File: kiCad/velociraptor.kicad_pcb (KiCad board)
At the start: 2 copper layers, 218 x 86.6 mm, 125 parts, among them J0 Conn_01x03, SW0 MX, SW1 MX, SW10 MX, SW11 MX, SW12 MX, SW13 MX, SW14 MX, SW15 MX, SW16 MX, SW17 MX, SW18 MX, SW19 MX, SW2 MX, SW20 MX, SW21 MX, SW22 MX, SW23 MX, SW24 MX, SW25 MX, SW26 MX, SW27 MX, SW28 MX, SW29 MX, SW3 MX, SW30 MX, SW31 MX, SW32 MX, SW33 MX, SW34 MX, SW35 MX, SW36 MX, SW37 MX, SW38 MX, SW39 MX, SW4 MX, SW40 MX, SW41 MX, SW42 MX, SW43 MX, SW44 MX, SW45 MX, SW46 MX, SW47 MX, SW48 MX, SW49 MX, SW5 MX, SW50 MX, SW51 MX, SW52 MX, SW53 MX, SW54 MX, SW55 MX, SW56 MX, SW57 MX, SW58 MX, SW59 MX, SW6 MX, SW61 MX, SW7 MX, SW8 MX, SW9 MX, U0 Sparkfun_Pro_Micro

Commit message: remove unused libraries, update to kicad 7, cleanup silkscreens
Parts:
- added ?: , , F.Cu at (232.5, 94.4)
- added ?: , , F.Cu at (51.9, 94.4)
- added ?: , , F.Cu at (51.9, 43.2)
- added ?: , , F.Cu at (142.3, 60.3)
- added ?: , , F.Cu at (232.5, 43.2)
- added ?: , , F.Cu at (142.3, 94.4)
- moved G*** 0.26 mm to (210.5, 90.7)
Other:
- board text added: "Velociraptor PCB by SylivanKenobi"

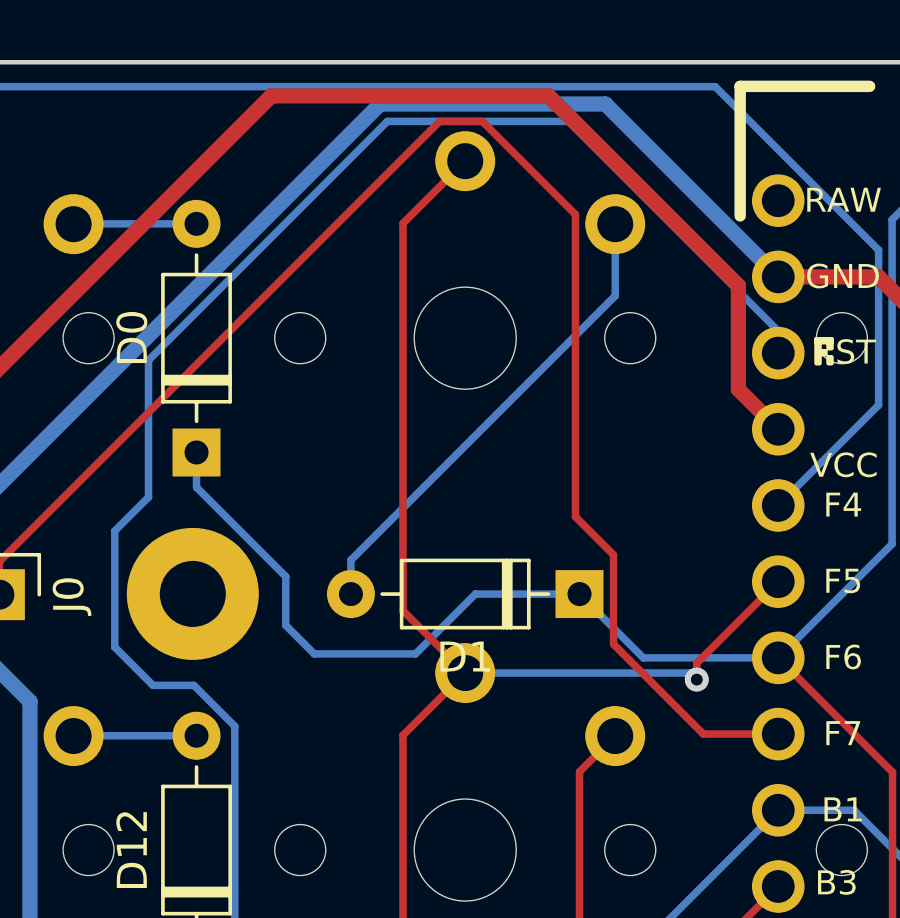
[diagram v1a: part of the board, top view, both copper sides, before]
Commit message: fix diode orientation
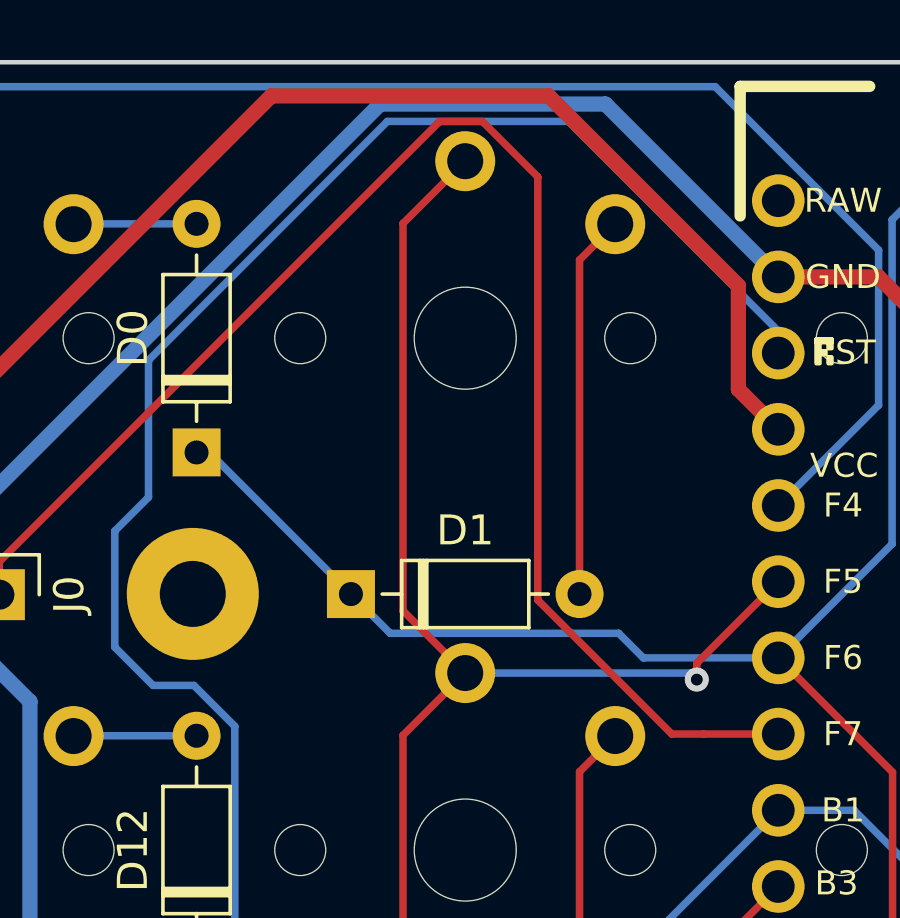
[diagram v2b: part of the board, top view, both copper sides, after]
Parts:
- moved D1 7.62 mm to (57.2, 43.2), turned to 0 degrees
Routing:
- net /ROW0: track 228.1 -> 224.8 mm
- net Net-(D1-A): track 16.0 -> 12.8 mm
- net /PIN15: track 49.2 -> 49.9 mm
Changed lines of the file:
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@@
   (net 82 "unconnected-(U0-RAW-Pad24)")
   (footprint "Diode_THT:D_DO-35_SOD27_P7.62mm_Horizontal" (layer "F.Cu")
-    (at 64.816199 43.23 180)
+    (at 57.196199 43.23)
     (descr "Diode, DO-35_SOD27 series, Axial, Horizontal, pin pitch=7.62mm, , length*diameter=4*2mm^2, , http://www.diodes.com/_files/packages/DO-35.pdf")
     (tags "Diode DO-35_SOD27 series Axial Horizontal pin pitch 7.62mm  length 4mm diameter 2mm")
@@
     (fp_line (start 7.62 0) (end 5.81 0)
       (stroke (width 0.1) (type solid)) (layer "F.Fab"))
-    (pad "1" thru_hole rect (at 0 0 180) (size 1.6 1.6) (drill 0.8) (layers "*.Cu" "*.Mask")
+    (pad "1" thru_hole rect (at 0 0) (size 1.6 1.6) (drill 0.8) (layers "*.Cu" "*.Mask")
       (net 16 "/ROW0") (pinfunction "K") (pintype "passive"))
-    (pad "2" thru_hole oval (at 7.62 0 180) (size 1.6 1.6) (drill 0.8) (layers "*.Cu" "*.Mask")
+    (pad "2" thru_hole oval (at 7.62 0) (size 1.6 1.6) (drill 0.8) (layers "*.Cu" "*.Mask")
       (net 22 "Net-(D1-A)") (pinfunction "A") (pintype "passive"))
     (model "${KICAD6_3DMODEL_DIR}/Diode_THT.3dshapes/D_DO-35_SOD27_P7.62mm_Horizontal.wrl"
@@
     (effects (font (size 1.5 1.5) (thickness 0.3) bold) (justify left bottom mirror))
   )
-  (dimension (type aligned) (layer "F.Cu")
-    (pts (xy 248.866202 112.147453) (xy 248.866202 25.502547))
-    (height 8.908798)
-    (gr_text "86.6449 mm" (at 255.975 68.825 90) (layer "F.Cu")
-      (effects (font (size 1.5 1.5) (thickness 0.3)))
+  (dimension (type aligned) (layer "Dwgs.User")
+    (pts (xy 232.495619 94.3875) (xy 142.278099 94.3875))
+    (height -24.7125)
+    (gr_text "90.2175 mm" (at 187.386859 117.95) (layer "Dwgs.User")
+      (effects (font (size 1 1) (thickness 0.15)))
+    )
+    (format (prefix "") (suffix "") (units 3) (units_format 1) (precision 4))
+    (style (thickness 0.15) (arrow_length 1.27) (text_position_mode 0) (extension_height 0.58642) (extension_offset 0.5) keep_text_aligned)
+  )
+  (dimension (type aligned) (layer "Dwgs.User")
+    (pts (xy 248.866202 25.502547) (xy 248.866202 112.147453))
+    (height -27.858798)
+    (gr_text "86.6449 mm" (at 275.575 68.825 90) (layer "Dwgs.User")
+      (effects (font (size 1 1) (thickness 0.15)))
+    )
+    (format (prefix "") (suffix "") (units 3) (units_format 1) (precision 4))
+    (style (thickness 0.15) (arrow_length 1.27) (text_position_mode 0) (extension_height 0.58642) (extension_offset 0.5) keep_text_aligned)
+  )
+  (dimension (type aligned) (layer "Dwgs.User")
+    (pts (xy 142.223719 60.2625) (xy 142.278099 94.45))
+    (height -119.168239)
+    (gr_text "34.1875 mm" (at 262.568996 77.164867 270.0911369) (layer "Dwgs.User")
+      (effects (font (size 1 1) (thickness 0.15)))
+    )
+    (format (prefix "") (suffix "") (units 3) (units_format 1) (precision 4))
+    (style (thickness 0.15) (arrow_length 1.27) (text_position_mode 0) (extension_height 0.58642) (extension_offset 0.5) keep_text_aligned)
+  )
+  (dimension (type aligned) (layer "Dwgs.User")
+    (pts (xy 232.549999 94.45) (xy 51.951819 94.45))
+    (height -32.375)
+    (gr_text "180.5982 mm" (at 142.250909 125.675) (layer "Dwgs.User")
+      (effects (font (size 1 1) (thickness 0.15)))
+    )
+    (format (prefix "") (suffix "") (units 3) (units_format 1) (precision 4))
+    (style (thickness 0.15) (arrow_length 1.27) (text_position_mode 0) (extension_height 0.58642) (extension_offset 0.5) keep_text_aligned)
+  )
+  (dimension (type aligned) (layer "Dwgs.User")
+    (pts (xy 232.525 43.225) (xy 232.495619 94.3875))
+    (height -39.730199)
+    (gr_text "51.1625 mm" (at 271.090501 68.828406 89.96709574) (layer "Dwgs.User")
+      (effects (font (size 1 1) (thickness 0.15)))
     )
     (format (prefix "") (suffix "") (units 3) (units_format 1) (precision 4))
-    (style (thickness 0.2) (arrow_length 1.27) (text_position_mode 0) (extension_height 0.58642) (extension_offset 0.5) keep_text_aligned)
+    (style (thickness 0.15) (arrow_length 1.27) (text_position_mode 0) (extension_height 0.58642) (extension_offset 0.5) keep_text_aligned)
   )
-  (dimension (type aligned) (layer "F.Cu")
-    (pts (xy 33.254367 109.766202) (xy 251.247452 109.766203))
-    (height 14.558797)
-    (gr_text "217.9931 mm" (at 142.25091 122.525 359.9999995) (layer "F.Cu")
-      (effects (font (size 1.5 1.5) (thickness 0.3)))
+  (dimension (type aligned) (layer "Dwgs.User")
+    (pts (xy 251.247452 109.766203) (xy 33.254367 109.766202))
+    (height -24.983123)
+    (gr_text "217.9931 mm" (at 142.250909 133.599325 -5.256659961e-07) (layer "Dwgs.User")
+      (effects (font (size 1 1) (thickness 0.15)))
     )
     (format (prefix "") (suffix "") (units 3) (units_format 1) (precision 4))
-    (style (thickness 0.2) (arrow_length 1.27) (text_position_mode 0) (extension_height 0.58642) (extension_offset 0.5) keep_text_aligned)
+    (style (thickness 0.15) (arrow_length 1.27) (text_position_mode 0) (extension_height 0.58642) (extension_offset 0.5) keep_text_aligned)
   )
   (segment (start 39.15 32.601819) (end 42.951819 28.8) (width 0.25) (layer "F.Cu") (net 1))
@@
   (segment (start 68.94675 47.89675) (end 71.440579 47.89675) (width 0.25) (layer "F.Cu") (net 13))
   (segment (start 45.476819 43.25) (end 45.476819 42.15) (width 0.25) (layer "F.Cu") (net 13))
-  (segment (start 64.681199 30.581199) (end 64.681199 40.656199) (width 0.25) (layer "F.Cu") (net 13))
+  (segment (start 61.575 27.475) (end 63.425 29.325) (width 0.25) (layer "F.Cu") (net 13))
   (segment (start 45.476819 42.15) (end 60.151819 27.475) (width 0.25) (layer "F.Cu") (net 13))
+  (segment (start 63.425 43.429792) (end 67.891958 47.89675) (width 0.25) (layer "F.Cu") (net 13))
+  (segment (start 67.891958 47.89675) (end 68.94675 47.89675) (width 0.25) (layer "F.Cu") (net 13))
+  (segment (start 63.425 29.325) (end 63.425 43.429792) (width 0.25) (layer "F.Cu") (net 13))
   (segment (start 60.151819 27.475) (end 61.575 27.475) (width 0.25) (layer "F.Cu") (net 13))
-  (segment (start 65.95 44.9) (end 68.94675 47.89675) (width 0.25) (layer "F.Cu") (net 13))
-  (segment (start 65.95 41.925) (end 65.95 44.9) (width 0.25) (layer "F.Cu") (net 13))
-  (segment (start 61.575 27.475) (end 64.681199 30.581199) (width 0.25) (layer "F.Cu") (net 13))
-  (segment (start 64.681199 40.656199) (end 65.95 41.925) (width 0.25) (layer "F.Cu") (net 13))
   (segment (start 75.95 33.825) (end 74.78175 32.65675) (width 0.508) (layer "F.Cu") (net 14))
   (segment (start 74.78175 32.65675) (end 71.440579 32.65675) (width 0.508) (layer "F.Cu") (net 14))
@@
   (segment (start 97.476429 38.51) (end 86.441429 27.475) (width 0.25) (layer "B.Cu") (net 16))
   (segment (start 75.23558 41.561749) (end 75.23558 30.751166) (width 0.25) (layer "B.Cu") (net 16))
-  (segment (start 52.05 38.51) (end 52.05 39.672911) (width 0.25) (layer "B.Cu") (net 16))
   (segment (start 233.024999 38.51) (end 237.739999 43.225) (width 0.25) (layer "B.Cu") (net 16))
+  (segment (start 66.942949 45.35675) (end 66.123699 44.5375) (width 0.25) (layer "B.Cu") (net 16))
+  (segment (start 52.476199 38.51) (end 57.196199 43.23) (width 0.25) (layer "B.Cu") (net 16))
   (segment (start 232.525 38.51) (end 106.125 38.51) (width 0.25) (layer "B.Cu") (net 16))
+  (segment (start 66.123699 44.5375) (end 58.503699 44.5375) (width 0.25) (layer "B.Cu") (net 16))
   (segment (start 71.440579 45.35675) (end 75.23558 41.561749) (width 0.25) (layer "B.Cu") (net 16))
-  (segment (start 61.345 43.23) (end 64.816199 43.23) (width 0.25) (layer "B.Cu") (net 16))
+  (segment (start 52.05 38.51) (end 52.476199 38.51) (width 0.25) (layer "B.Cu") (net 16))
   (segment (start 106.125 38.51) (end 97.476429 38.51) (width 0.25) (layer "B.Cu") (net 16))
-  (segment (start 55.975 45.225) (end 59.35 45.225) (width 0.25) (layer "B.Cu") (net 16))
-  (segment (start 59.35 45.225) (end 61.345 43.23) (width 0.25) (layer "B.Cu") (net 16))
-  (segment (start 66.942949 45.35675) (end 64.816199 43.23) (width 0.25) (layer "B.Cu") (net 16))
   (segment (start 86.441429 27.475) (end 78.675 27.475) (width 0.25) (layer "B.Cu") (net 16))
-  (segment (start 55.025 42.647911) (end 55.025 44.275) (width 0.25) (layer "B.Cu") (net 16))
-  (segment (start 55.025 44.275) (end 55.975 45.225) (width 0.25) (layer "B.Cu") (net 16))
   (segment (start 71.440579 45.35675) (end 66.942949 45.35675) (width 0.25) (layer "B.Cu") (net 16))
-  (segment (start 52.05 39.672911) (end 55.025 42.647911) (width 0.25) (layer "B.Cu") (net 16))
   (segment (start 75.23558 30.751166) (end 78.511746 27.475) (width 0.25) (layer "B.Cu") (net 16))
+  (segment (start 58.503699 44.5375) (end 57.196199 43.23) (width 0.25) (layer "B.Cu") (net 16))
   (segment (start 101.4 61.425) (end 100.275 61.425) (width 0.25) (layer "B.Cu") (net 17))
   (segment (start 57.196199 60.3) (end 55.752847 60.3) (width 0.25) (layer "B.Cu") (net 17))
@@
   (segment (start 47.961819 30.89) (end 47.951819 30.9) (width 0.25) (layer "B.Cu") (net 21))
   (segment (start 52.05 30.89) (end 47.961819 30.89) (width 0.25) (layer "B.Cu") (net 21))
-  (segment (start 66.006199 33.28863) (end 66.006199 30.9) (width 0.25) (layer "B.Cu") (net 22))
-  (segment (start 57.196199 43.23) (end 57.196199 42.09863) (width 0.25) (layer "B.Cu") (net 22))
-  (segment (start 57.196199 42.09863) (end 66.006199 33.28863) (width 0.25) (layer "B.Cu") (net 22))
+  (segment (start 66.006199 30.9) (end 64.816199 32.09) (width 0.25) (layer "F.Cu") (net 22))
+  (segment (start 64.816199 32.09) (end 64.816199 43.23) (width 0.25) (layer "F.Cu") (net 22))
   (segment (start 82.870579 60.3) (end 82.07058 59.500001) (width 0.25) (layer "F.Cu") (net 23))
   (segment (start 82.07058 59.500001) (end 82.07058 32.889999) (width 0.25) (layer "F.Cu") (net 23))
